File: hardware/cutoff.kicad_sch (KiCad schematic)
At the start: 9 parts, among them Q7 AO3401A, Q8 2N7002

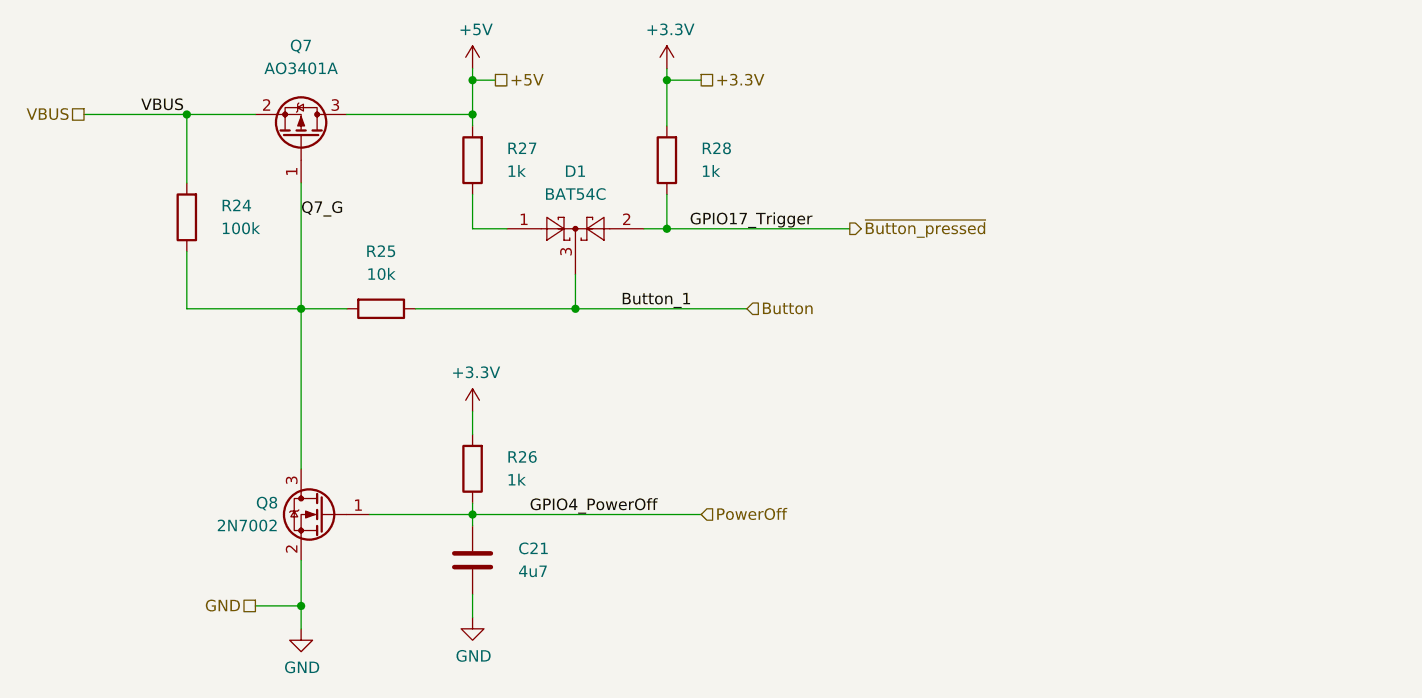
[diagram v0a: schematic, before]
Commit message: Fix all ERC warnings. Replace 4u7 capacitor in cut-off circuit by 100 nF cap and 10 kOhm in series to reduce stress on Raspi GPIO.
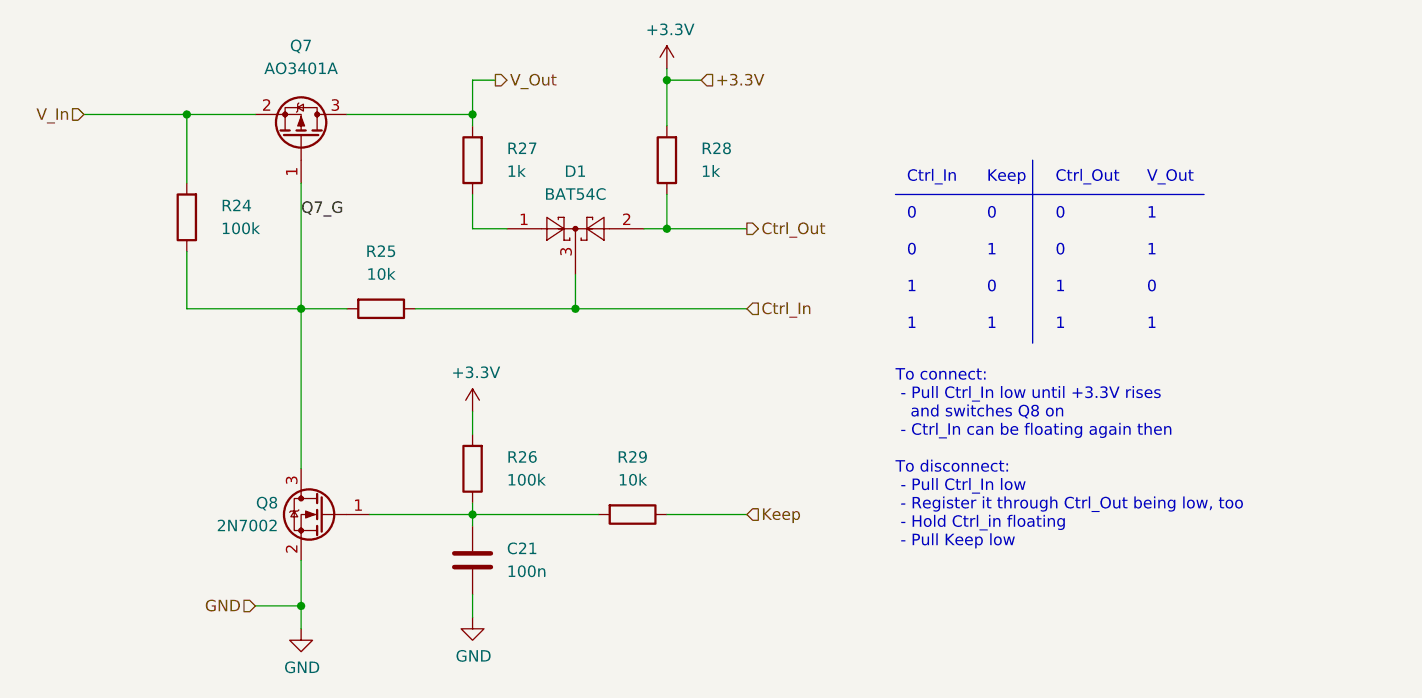
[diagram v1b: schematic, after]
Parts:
- added R29: 10k, Resistor_SMD:R_0603_1608Metric, symbol Device:R
- C21: value 4u7 -> 100n
- R26: value 1k -> 100k
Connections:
- net +3V3 renamed +3.3V
- net +5V renamed V_Out
- net Button renamed Ctrl_In
- net PowerOff: no longer names the net of C21.1, Q8.1 (G), R26.1
- net PowerOff: now also R29.2
- net VBUS renamed V_In
- net ~{Button_pressed} renamed Ctrl_Out
- new net Keep: R29.1
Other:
- note added: "Ctrl_In 0 0 1 1"
- note added: "Ctrl_Out 0 0 1 1"
- note added: "Keep 0 1 0 1"
- note added: "To connect: - Pull Ctrl_In low until +3.3V rises and switches Q8 on - Ctrl_In can be floating again then To disconnect: - Pull Ctrl_In low - Register it through Ctrl_Out being low, too - Hold Ctrl_in floating - Pull Keep low"
- note added: "V_Out 1 1 0 1"
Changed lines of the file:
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@@
   (junction (at 104.14 62.23) (diameter 0) (color 0 0 0 0)
   )
-  (junction (at 135.89 58.42) (diameter 0) (color 0 0 0 0)
-  )
   (junction (at 135.89 106.68) (diameter 0) (color 0 0 0 0)
   )
@@
     (stroke (width 0) (type default) (color 0 0 0 0))
   )
+  (polyline (pts (xy 198.12 67.31) (xy 198.12 87.63))
+    (stroke (width 0) (type default) (color 0 0 0 0))
+  )
   (wire (pts (xy 157.48 71.12) (xy 157.48 74.93))
     (stroke (width 0) (type default) (color 0 0 0 0))
   )
-  (wire (pts (xy 157.48 74.93) (xy 177.8 74.93))
+  (wire (pts (xy 157.48 74.93) (xy 166.37 74.93))
     (stroke (width 0) (type default) (color 0 0 0 0))
   )
@@
     (stroke (width 0) (type default) (color 0 0 0 0))
   )
+  (wire (pts (xy 157.48 106.68) (xy 166.37 106.68))
+    (stroke (width 0) (type default) (color 0 0 0 0))
+  )
   (wire (pts (xy 121.92 83.82) (xy 116.84 83.82))
     (stroke (width 0) (type default) (color 0 0 0 0))
   )
+  (polyline (pts (xy 182.88 71.12) (xy 217.17 71.12))
+    (stroke (width 0) (type default) (color 0 0 0 0))
+  )
   (wire (pts (xy 135.89 106.68) (xy 135.89 107.95))
     (stroke (width 0) (type default) (color 0 0 0 0))
@@
     (stroke (width 0) (type default) (color 0 0 0 0))
   )
+  (wire (pts (xy 135.89 106.68) (xy 149.86 106.68))
+    (stroke (width 0) (type default) (color 0 0 0 0))
+  )
   (wire (pts (xy 104.14 77.47) (xy 104.14 83.82))
     (stroke (width 0) (type default) (color 0 0 0 0))
@@
     (stroke (width 0) (type default) (color 0 0 0 0))
   )
-  (wire (pts (xy 135.89 57.15) (xy 135.89 58.42))
-    (stroke (width 0) (type default) (color 0 0 0 0))
-  )
   (wire (pts (xy 135.89 62.23) (xy 135.89 63.5))
     (stroke (width 0) (type default) (color 0 0 0 0))
@@
     (stroke (width 0) (type default) (color 0 0 0 0))
   )
-  (wire (pts (xy 135.89 106.68) (xy 161.29 106.68))
-    (stroke (width 0) (type default) (color 0 0 0 0))
-  )
   (wire (pts (xy 135.89 115.57) (xy 135.89 118.11))
     (stroke (width 0) (type default) (color 0 0 0 0))
@@
     (stroke (width 0) (type default) (color 0 0 0 0))
   )
-  (label "Button_1" (at 152.4 83.82 0)
+  (text "Ctrl_In\n\n0\n\n0\n\n1\n\n1" (at 184.15 86.36 0)
+    (effects (font (size 1.27 1.27)) (justify left bottom))
+  )
+  (text "V_Out\n\n1\n\n1\n\n0\n\n1" (at 210.82 86.36 0)
+    (effects (font (size 1.27 1.27)) (justify left bottom))
+  )
+  (text "Keep\n\n0\n\n1\n\n0\n\n1" (at 193.04 86.36 0)
+    (effects (font (size 1.27 1.27)) (justify left bottom))
+  )
+  (text "Ctrl_Out\n\n0\n\n0\n\n1\n\n1" (at 200.66 86.36 0)
+    (effects (font (size 1.27 1.27)) (justify left bottom))
+  )
+  (text "To connect:\n - Pull Ctrl_In low until +3.3V rises\n   and switches Q8 on\n - Ctrl_In can be floating again then\n\nTo disconnect:\n - Pull Ctrl_In low\n - Register it through Ctrl_Out being low, too\n - Hold Ctrl_in floating\n - Pull Keep low "
+    (at 182.88 110.49 0)
     (effects (font (size 1.27 1.27)) (justify left bottom))
   )
@@
     (effects (font (size 1.27 1.27)) (justify left bottom))
   )
-  (label "VBUS" (at 99.06 62.23 0)
-    (effects (font (size 1.27 1.27)) (justify left bottom))
-  )
-  (label "GPIO4_PowerOff" (at 142.24 106.68 0)
-    (effects (font (size 1.27 1.27)) (justify left bottom))
-  )
-  (label "GPIO17_Trigger" (at 160.02 74.93 0)
-    (effects (font (size 1.27 1.27)) (justify left bottom))
-  )
-  (hierarchical_label "Button" (shape input) (at 166.37 83.82 0)
-    (effects (font (size 1.27 1.27)) (justify left))
-  )
-  (hierarchical_label "+3.3V" (shape passive) (at 161.29 58.42 0)
-    (effects (font (size 1.27 1.27)) (justify left))
-  )
-  (hierarchical_label "PowerOff" (shape input) (at 161.29 106.68 0)
-    (effects (font (size 1.27 1.27)) (justify left))
-  )
-  (hierarchical_label "+5V" (shape passive) (at 138.43 58.42 0)
-    (effects (font (size 1.27 1.27)) (justify left))
-  )
-  (hierarchical_label "VBUS" (shape passive) (at 92.71 62.23 180)
+  (hierarchical_label "Ctrl_In" (shape input) (at 166.37 83.82 0)
+    (effects (font (size 1.27 1.27)) (justify left))
+  )
+  (hierarchical_label "+3.3V" (shape input) (at 161.29 58.42 0)
+    (effects (font (size 1.27 1.27)) (justify left))
+  )
+  (hierarchical_label "Keep" (shape input) (at 166.37 106.68 0)
+    (effects (font (size 1.27 1.27)) (justify left))
+  )
+  (hierarchical_label "V_Out" (shape output) (at 138.43 58.42 0)
+    (effects (font (size 1.27 1.27)) (justify left))
+  )
+  (hierarchical_label "V_In" (shape input) (at 92.71 62.23 180)
     (effects (font (size 1.27 1.27)) (justify right))
   )
-  (hierarchical_label "~{Button_pressed}" (shape output) (at 177.8 74.93 0)
-    (effects (font (size 1.27 1.27)) (justify left))
-  )
-  (hierarchical_label "GND" (shape passive) (at 111.76 116.84 180)
+  (hierarchical_label "Ctrl_Out" (shape output) (at 166.37 74.93 0)
+    (effects (font (size 1.27 1.27)) (justify left))
+  )
+  (hierarchical_label "GND" (shape input) (at 111.76 116.84 180)
     (effects (font (size 1.27 1.27)) (justify right))
   )
-  (symbol (lib_id "power:+5V") (at 135.89 57.15 0) (unit 1)
-    (in_bom yes) (on_board yes)
-    (property "Reference" "#PWR0158" (id 0) (at 135.89 60.96 0)
-      (effects (font (size 1.27 1.27)) hide)
-    )
-    (property "Value" "+5V" (id 1) (at 136.2583 52.8256 0))
-    (property "Footprint" "" (id 2) (at 135.89 57.15 0))
-    (property "Datasheet" "" (id 3) (at 135.89 57.15 0))
-    (pin "1")
+  (symbol (lib_id "Device:R") (at 153.67 106.68 270) (unit 1)
+    (in_bom yes) (on_board yes) (fields_autoplaced)
+    (property "Reference" "R29" (id 0) (at 153.67 100.33 90))
+    (property "Value" "10k" (id 1) (at 153.67 102.87 90))
+    (property "Footprint" "Resistor_SMD:R_0603_1608Metric" (id 2) (at 153.67 104.902 90)
+      (effects (font (size 1.27 1.27)) hide)
+    )
+    (property "Datasheet" "~" (id 3) (at 153.67 106.68 0)
+      (effects (font (size 1.27 1.27)) hide)
+    )
+    (property "Comment" "5% 100ppm" (id 4) (at 153.67 106.68 0)
+      (effects (font (size 1.27 1.27)) hide)
+    )
+    (pin "1")
+    (pin "2")
   )
   (symbol (lib_id "Device:R") (at 135.89 101.6 180) (unit 1)
@@
       (effects (font (size 1.27 1.27)) (justify right))
     )
-    (property "Value" "1k" (id 1) (at 139.7 102.8699 0)
+    (property "Value" "100k" (id 1) (at 139.7 102.8699 0)
       (effects (font (size 1.27 1.27)) (justify right))
     )
@@
   (symbol (lib_id "Device:C") (at 135.89 111.76 0) (unit 1)
     (in_bom yes) (on_board yes) (fields_autoplaced)
-    (property "Reference" "C21" (id 0) (at 140.97 110.4899 0)
+    (property "Reference" "C21" (id 0) (at 139.7 110.4899 0)
       (effects (font (size 1.27 1.27)) (justify left))
     )
-    (property "Value" "4u7" (id 1) (at 140.97 113.0299 0)
+    (property "Value" "100n" (id 1) (at 139.7 113.0299 0)
       (effects (font (size 1.27 1.27)) (justify left))
     )
@@
   (symbol (lib_id "power:GND") (at 116.84 119.38 0) (unit 1)
     (in_bom yes) (on_board yes)
-    (property "Reference" "#PWR0153" (id 0) (at 116.84 125.73 0)
+    (property "Reference" "#PWR05" (id 0) (at 116.84 125.73 0)
       (effects (font (size 1.27 1.27)) hide)
     )
@@
   (symbol (lib_id "power:GND") (at 135.89 118.11 0) (unit 1)
     (in_bom yes) (on_board yes)
-    (property "Reference" "#PWR0154" (id 0) (at 135.89 124.46 0)
+    (property "Reference" "#PWR07" (id 0) (at 135.89 124.46 0)
       (effects (font (size 1.27 1.27)) hide)
     )
@@
   (symbol (lib_id "power:+3.3V") (at 135.89 95.25 0) (unit 1)
     (in_bom yes) (on_board yes)
-    (property "Reference" "#PWR0155" (id 0) (at 135.89 99.06 0)
+    (property "Reference" "#PWR06" (id 0) (at 135.89 99.06 0)
       (effects (font (size 1.27 1.27)) hide)
     )
@@
   (symbol (lib_id "power:+3.3V") (at 157.48 57.15 0) (unit 1)
     (in_bom yes) (on_board yes)
-    (property "Reference" "#PWR0157" (id 0) (at 157.48 60.96 0)
-      (effects (font (size 1.27 1.27)) hide)
-    )
+    (property "Reference" "#PWR08" (id 0) (at 157.48 60.96 0)
+      (effects (font (size 1.27 1.27)) hide)
+    )
